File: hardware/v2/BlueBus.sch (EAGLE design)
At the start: 139 parts, among them J1 3PIN_953442_1, J2 6PIN_953442_1, J3 6PIN_5_103166_1, J4 SJ2-35853A-SMT-TR, J5 SMB_CONN, J6 USB3080-30-01-A, J7 PCM12SMTR, J8 TC2030NL, Q1 NMOSFET-BSS138K, Q2 NMOSFET-BSS138K, Q3 PMOSFET-DMP32D4SSOT323, U1 MPQ4420, U10 PCM5122, U11 PAM8406, U2 TH3122.4, U3 FT231XS, U4 S-1212BC0-U5T1U, U5 XC6210, U6 CAT25M01, U7 PIC24FJ1024GA606, U8 BM83SM1, U9 DIT4096

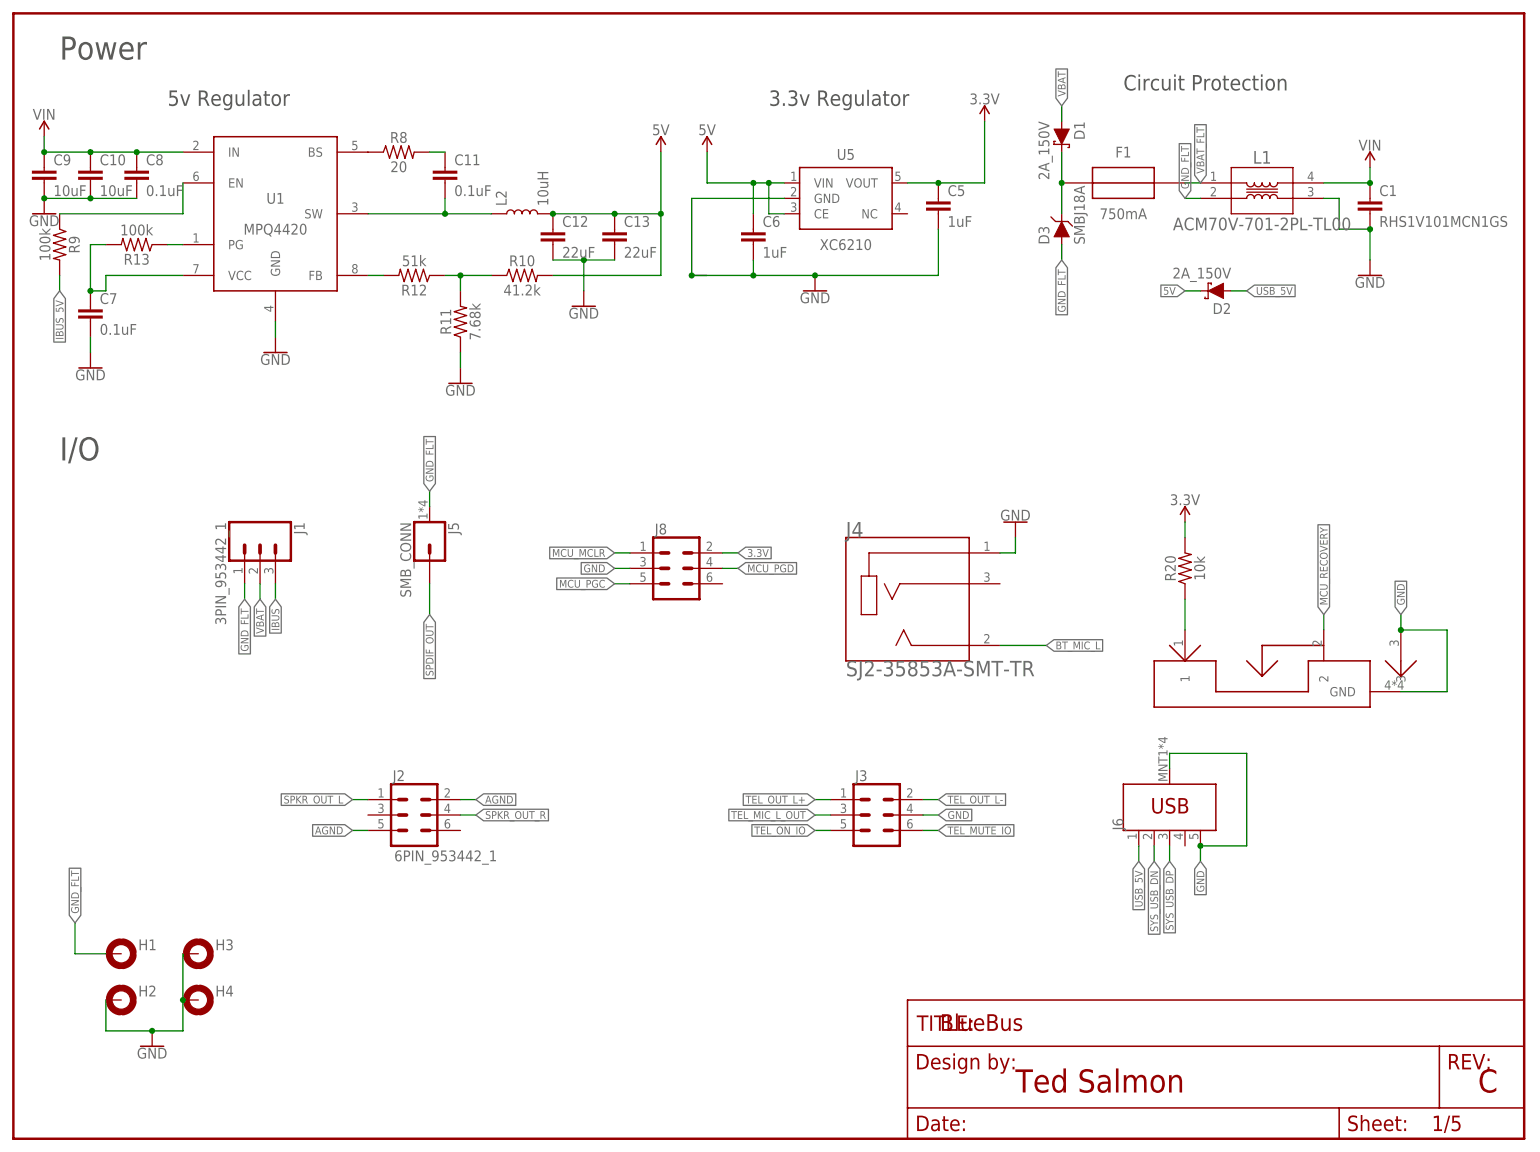
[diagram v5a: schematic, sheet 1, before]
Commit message: [IMP] hardware: V2 silkscreen * Add fiducial markings * Fix issues with silkscreen
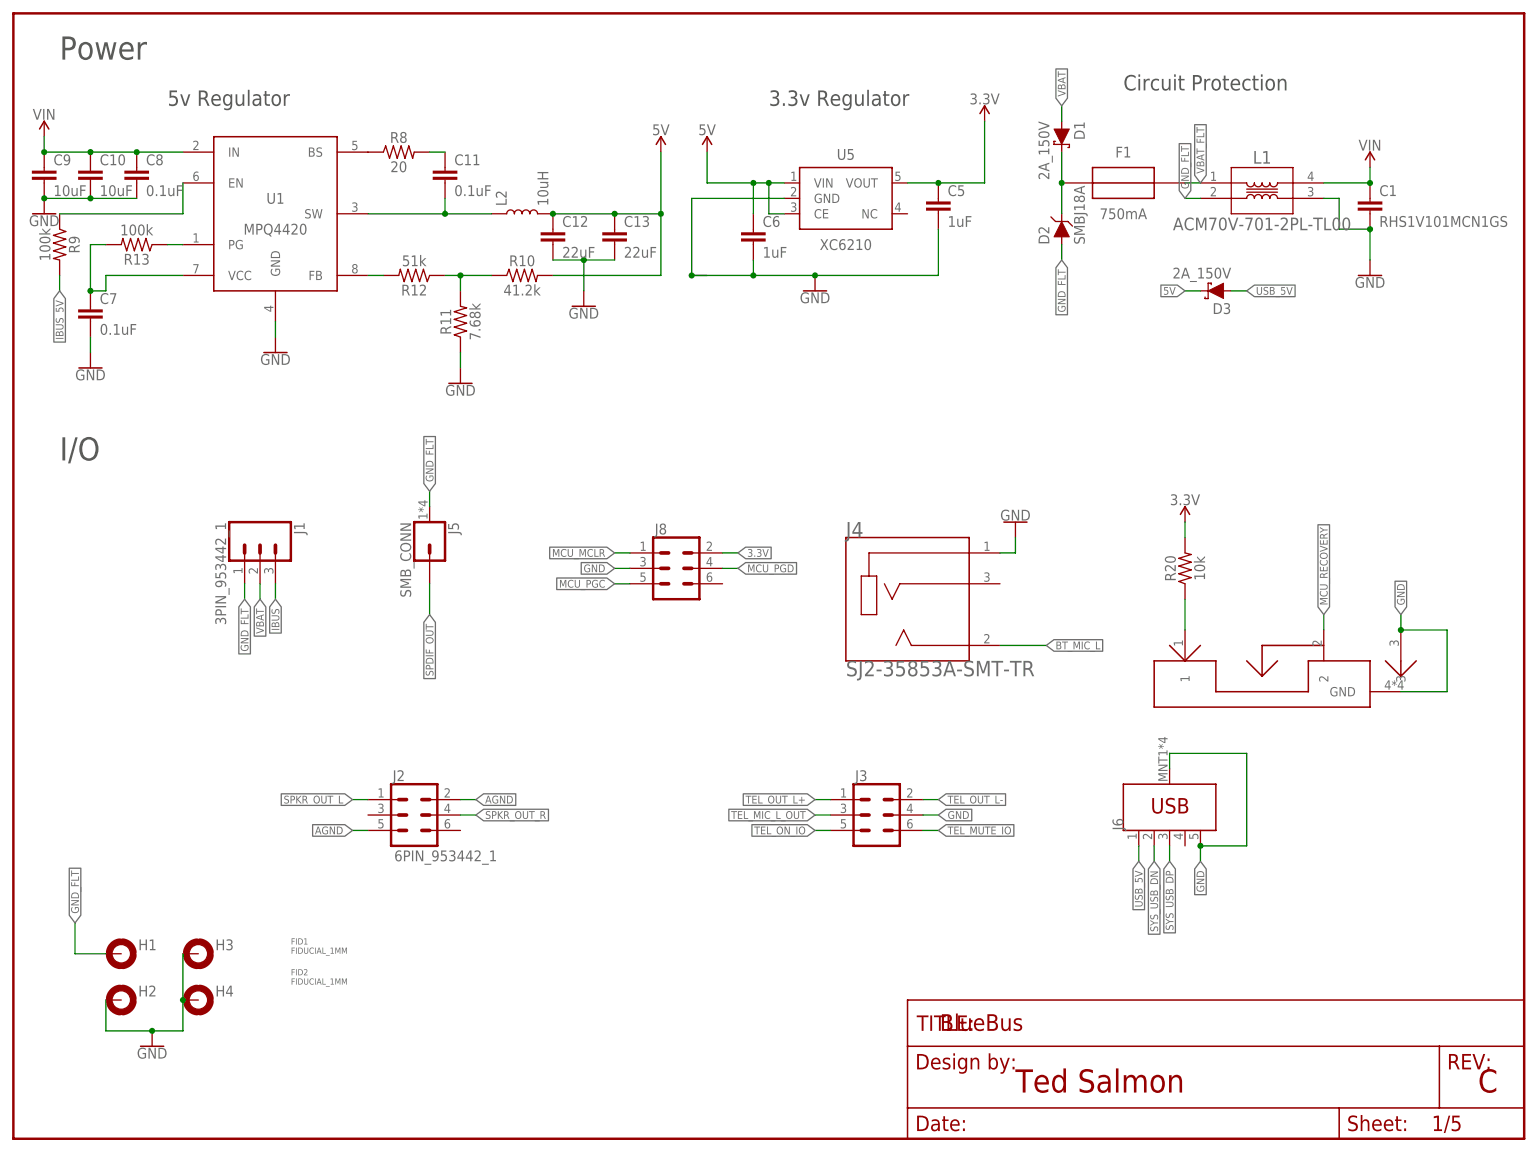
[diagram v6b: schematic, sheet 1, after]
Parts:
- added FID1, FID2: FIDUCIAL_1MM, MF_Aesthetics:FIDUCIAL_1MM
- D2: value 2A_150V -> SMBJ18A; device Passives:SMD2150PL_2A_150V -> Passives:SMBJ18A
- D3: value SMBJ18A -> 2A_150V; device Passives:SMBJ18A -> Passives:SMD2150PL_2A_150V
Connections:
- net 5V: now also D3.C; no longer D2.C
- net GND_FLT: now also D2.A; no longer D3.A
- net USB_5V: now also D3.A; no longer D2.A
- net VBAT_DIODE: now also D2.C; no longer D3.C
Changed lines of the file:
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@@
 <part name="GND8" library="SparkFun-PowerSymbols" library_urn="urn:adsk.eagle:library:530" deviceset="GND" device=""/>
 <part name="PWR" library="Passives" deviceset="LED_GREEN" device=""/>
-<part name="D2" library="Passives" deviceset="SMD2150PL_2A_150V" device="" value="2A_150V"/>
+<part name="D3" library="Passives" deviceset="SMD2150PL_2A_150V" device="" value="2A_150V"/>
 <part name="C61" library="Passives" deviceset="0.1UF" device="0603" value="0.1uF"/>
 <part name="C59" library="Passives" deviceset="0.1UF" device="0603" value="0.1uF"/>
@@
 <part name="R3" library="Passives" deviceset="1KOHM" device="0603" value="1k"/>
 <part name="GND41" library="SparkFun-PowerSymbols" library_urn="urn:adsk.eagle:library:530" deviceset="GND" device=""/>
-<part name="D3" library="Passives" deviceset="SMBJ18A" device=""/>
+<part name="D2" library="Passives" deviceset="SMBJ18A" device=""/>
+<part name="FID1" library="MF_Aesthetics" deviceset="FIDUCIAL" device="_1MM"/>
+<part name="FID2" library="MF_Aesthetics" deviceset="FIDUCIAL" device="_1MM"/>
 </parts>
 <sheets>
@@
 <attribute name="NAME" x="71.628" y="101.6" size="1.778" layer="95" font="vector" rot="R270"/>
 </instance>
-<instance part="D2" gate="G$1" x="198.12" y="139.7" smashed="yes" rot="R180">
+<instance part="D3" gate="G$1" x="198.12" y="139.7" smashed="yes" rot="R180">
 <attribute name="NAME" x="200.66" y="137.668" size="1.778" layer="95" font="vector" rot="R180"/>
 <attribute name="VALUE" x="200.66" y="141.732" size="1.778" layer="96" font="vector" rot="R180" align="top-left"/>
@@
 <attribute name="NAME" x="105.664" y="99.568" size="1.778" layer="95" font="vector"/>
 </instance>
-<instance part="D3" gate="G$1" x="172.72" y="149.86" smashed="yes" rot="R90">
+<instance part="D2" gate="G$1" x="172.72" y="149.86" smashed="yes" rot="R90">
 <attribute name="NAME" x="170.688" y="147.32" size="1.778" layer="95" font="vector" rot="R90"/>
 <attribute name="VALUE" x="174.752" y="147.32" size="1.778" layer="96" font="vector" rot="R90" align="top-left"/>
+</instance>
+<instance part="FID1" gate="G$1" x="45.72" y="33.02" smashed="yes">
+<attribute name="VALUE" x="45.72" y="31.496" size="1.016" layer="96" font="vector" rot="MR180"/>
+<attribute name="NAME" x="45.72" y="33.02" size="1.016" layer="95" font="vector" rot="MR180"/>
+</instance>
+<instance part="FID2" gate="G$1" x="45.72" y="27.94" smashed="yes">
+<attribute name="VALUE" x="45.72" y="26.416" size="1.016" layer="96" font="vector" rot="MR180"/>
+<attribute name="NAME" x="45.72" y="27.94" size="1.016" layer="95" font="vector" rot="MR180"/>
 </instance>
 </instances>
@@
 </segment>
 <segment>
-<pinref part="D2" gate="G$1" pin="C"/>
+<pinref part="D3" gate="G$1" pin="C"/>
 <wire x1="195.58" y1="139.7" x2="193.04" y2="139.7" width="0.1524" layer="91"/>
 <label x="193.04" y="139.7" size="1.27" layer="95" rot="R180" xref="yes"/>
@@
 </segment>
 <segment>
-<pinref part="D2" gate="G$1" pin="A"/>
+<pinref part="D3" gate="G$1" pin="A"/>
 <wire x1="200.66" y1="139.7" x2="203.2" y2="139.7" width="0.1524" layer="91"/>
 <label x="203.2" y="139.7" size="1.27" layer="95" xref="yes"/>
@@
 <wire x1="172.72" y1="157.48" x2="172.72" y2="152.4" width="0.1524" layer="91"/>
 <junction x="172.72" y="157.48"/>
-<pinref part="D3" gate="G$1" pin="C"/>
+<pinref part="D2" gate="G$1" pin="C"/>
 </segment>
 </net>
@@
 <segment>
 <wire x1="172.72" y1="147.32" x2="172.72" y2="144.78" width="0.1524" layer="91"/>
-<pinref part="D3" gate="G$1" pin="A"/>
+<pinref part="D2" gate="G$1" pin="A"/>
 <label x="172.72" y="144.78" size="1.27" layer="95" rot="R270" xref="yes"/>
 </segment>

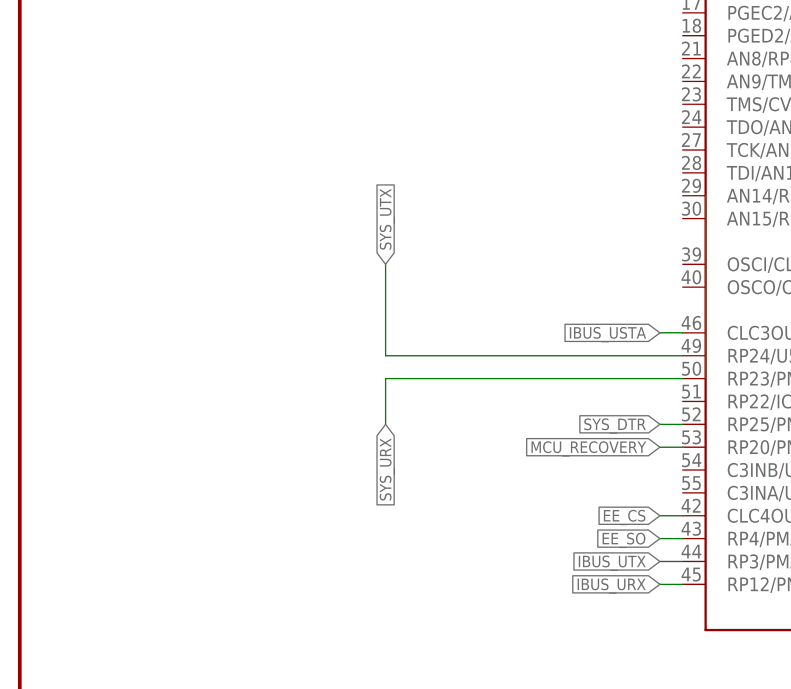
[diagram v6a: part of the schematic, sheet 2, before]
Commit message: [IMP] hardware: V2 System UART Fix * Swap URX/UTX pins to maintain the same mapping as 1.x boards
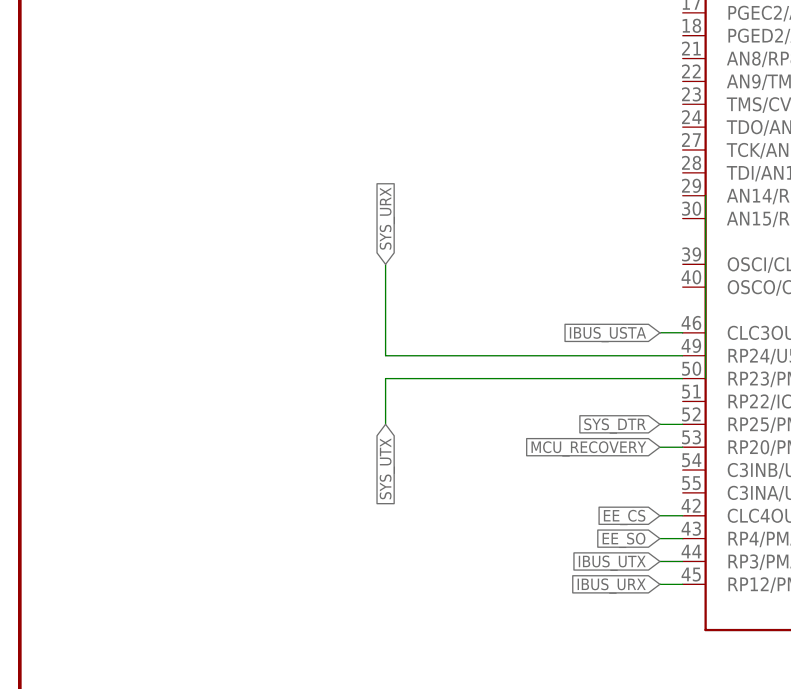
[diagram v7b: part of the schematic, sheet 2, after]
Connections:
- net SYS_URX: now also U7.RP24/U5TX/ICM4/RD1; no longer U7.RP23/PMACK1/RD2
- net SYS_UTX: now also U7.RP23/PMACK1/RD2; no longer U7.RP24/U5TX/ICM4/RD1
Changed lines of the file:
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@@
-</segment>
-</net>
-<net name="SYS_URX" class="5">
-<segment>
-<wire x1="73.66" y1="83.82" x2="40.64" y2="83.82" width="0.1524" layer="91"/>
-<label x="40.64" y="78.74" size="1.27" layer="95" rot="R270" xref="yes"/>
-<pinref part="U7" gate="G$1" pin="RP23/PMACK1/RD2"/>
-<wire x1="40.64" y1="83.82" x2="40.64" y2="78.74" width="0.1524" layer="91"/>
-</segment>
-</net>
-<net name="SYS_UTX" class="5">
-<segment>
-<wire x1="73.66" y1="86.36" x2="40.64" y2="86.36" width="0.1524" layer="91"/>
-<label x="40.64" y="96.52" size="1.27" layer="95" rot="R90" xref="yes"/>
-<pinref part="U7" gate="G$1" pin="RP24/U5TX/ICM4/RD1"/>
-<wire x1="40.64" y1="86.36" x2="40.64" y2="96.52" width="0.1524" layer="91"/>
 </segment>
 </net>
@@
 </segment>
 </net>
+<net name="SYS_URX" class="5">
+<segment>
+<wire x1="73.66" y1="86.36" x2="40.64" y2="86.36" width="0.1524" layer="91"/>
+<label x="40.64" y="96.52" size="1.27" layer="95" rot="R90" xref="yes"/>
+<pinref part="U7" gate="G$1" pin="RP24/U5TX/ICM4/RD1"/>
+<wire x1="40.64" y1="86.36" x2="40.64" y2="96.52" width="0.1524" layer="91"/>
+</segment>
+</net>
+<net name="SYS_UTX" class="5">
+<segment>
+<wire x1="73.66" y1="83.82" x2="40.64" y2="83.82" width="0.1524" layer="91"/>
+<label x="40.64" y="78.74" size="1.27" layer="95" rot="R270" xref="yes"/>
+<pinref part="U7" gate="G$1" pin="RP23/PMACK1/RD2"/>
+<wire x1="40.64" y1="83.82" x2="40.64" y2="78.74" width="0.1524" layer="91"/>
+</segment>
+</net>
